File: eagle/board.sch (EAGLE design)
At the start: 11 parts, among them J1 M20X2SHROUDED

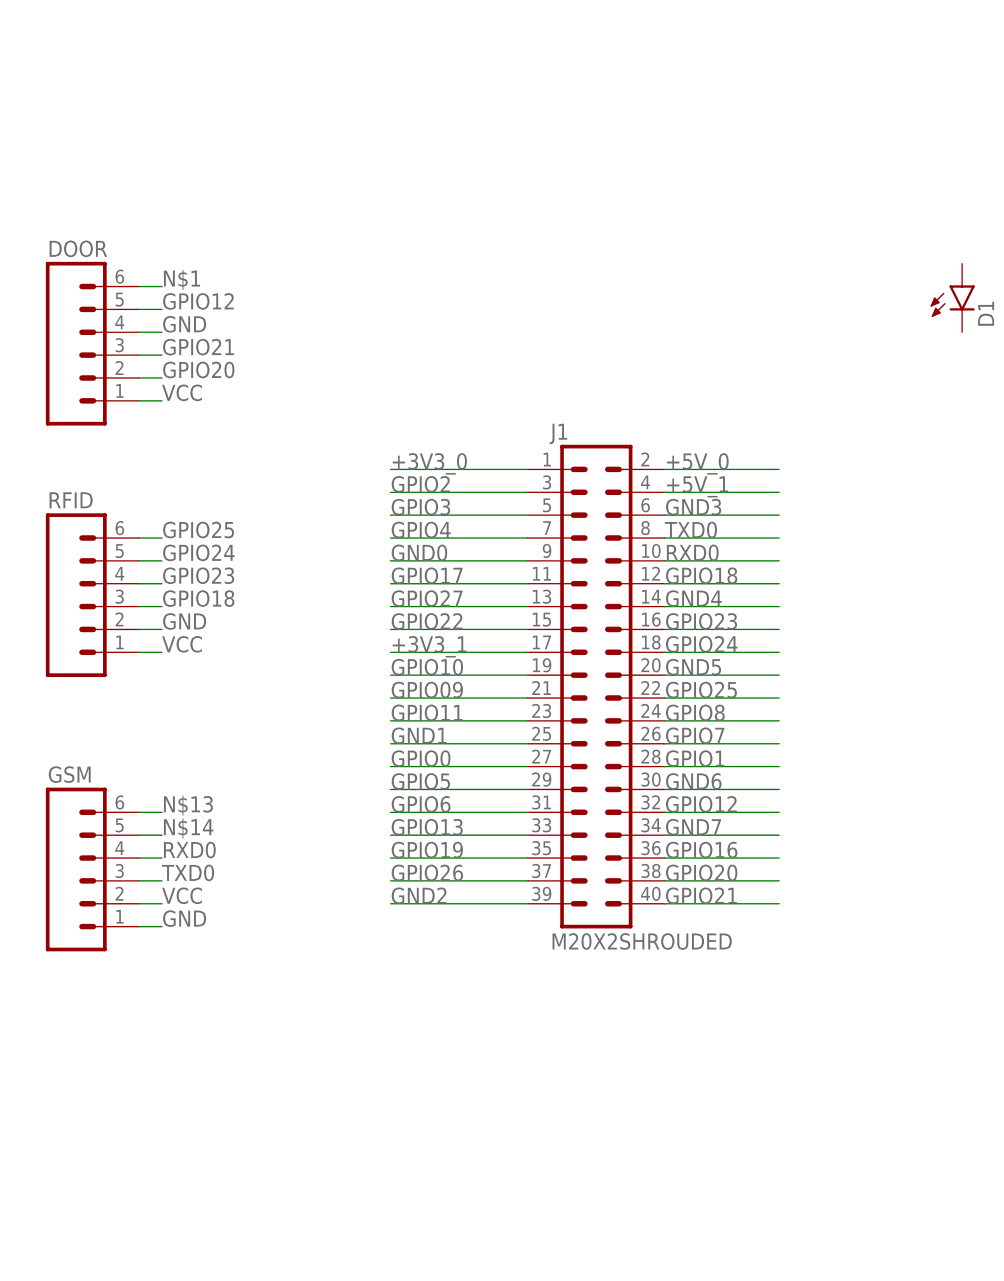
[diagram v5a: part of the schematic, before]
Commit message: Rename nets to match signal
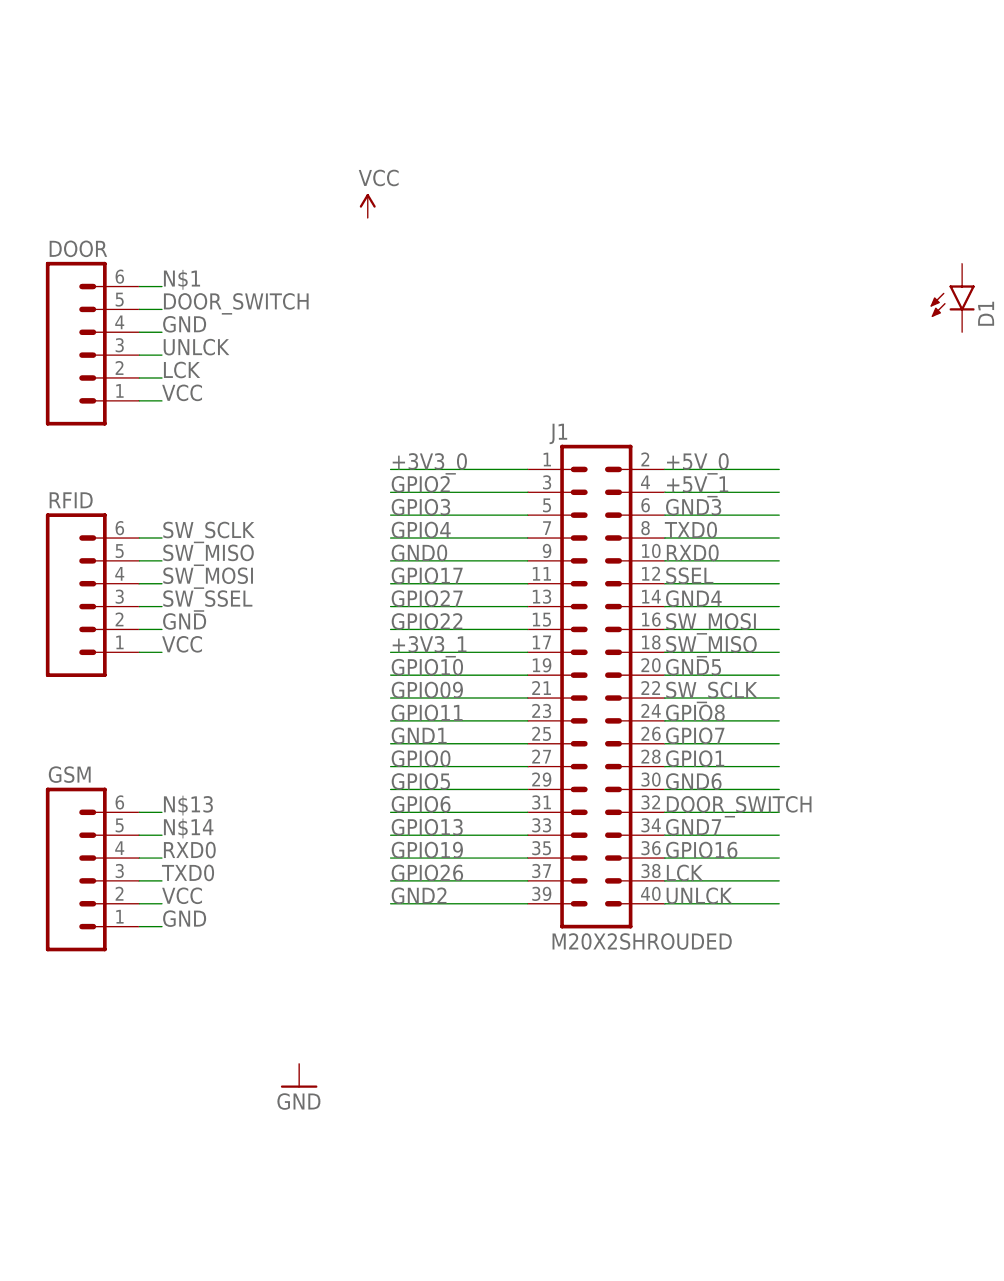
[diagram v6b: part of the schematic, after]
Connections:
- net GPIO12 renamed DOOR_SWITCH
- net GPIO20 renamed LCK
- net GPIO21 renamed UNLCK
- net GPIO23 renamed SW_MOSI
- net GPIO24 renamed SW_MISO
- net GPIO25 renamed SW_SCLK
- removed net GPIO18: J1.12, RFID.3
- new net SSEL: J1.12
- new net SW_SSEL: RFID.3
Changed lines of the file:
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@@
 <part name="C1" library="SparkFun-Passives" deviceset="CAP" device="PTH" value="10nF"/>
 <part name="C2" library="SparkFun-Passives" deviceset="CAP" device="PTH" value="10nF"/>
+<part name="SUPPLY1" library="SparkFun-Aesthetics" deviceset="VCC" device=""/>
+<part name="GND1" library="SparkFun-Aesthetics" deviceset="GND" device=""/>
 </parts>
 <sheets>
@@
 <instance part="C1" gate="G$1" x="119.38" y="55.88" rot="R270"/>
 <instance part="C2" gate="G$1" x="187.96" y="53.34" rot="R90"/>
+<instance part="SUPPLY1" gate="G$1" x="43.18" y="142.24"/>
+<instance part="GND1" gate="1" x="35.56" y="45.72"/>
 </instances>
 <busses>
@@
 </segment>
 </net>
-<net name="GPIO18" class="0">
+<net name="SSEL" class="0">
 <segment>
 <pinref part="J1" gate="G$1" pin="12"/>
@@
 <label x="76.2" y="101.6" size="1.778" layer="95"/>
 </segment>
-<segment>
-<pinref part="RFID" gate="G$1" pin="3"/>
-<wire x1="17.78" y1="99.06" x2="20.32" y2="99.06" width="0.1524" layer="91"/>
-<label x="20.32" y="99.06" size="1.778" layer="95"/>
-</segment>
-</net>
-<net name="GPIO23" class="0">
+</net>
+<net name="SW_MOSI" class="0">
 <segment>
 <pinref part="J1" gate="G$1" pin="16"/>
@@
 </segment>
 </net>
-<net name="GPIO24" class="0">
+<net name="SW_MISO" class="0">
 <segment>
 <pinref part="J1" gate="G$1" pin="18"/>
@@
 </segment>
 </net>
-<net name="GPIO25" class="0">
+<net name="SW_SCLK" class="0">
 <segment>
 <pinref part="J1" gate="G$1" pin="22"/>
@@
 </segment>
 </net>
-<net name="GPIO12" class="0">
+<net name="DOOR_SWITCH" class="0">
 <segment>
 <pinref part="J1" gate="G$1" pin="32"/>
@@
 </segment>
 </net>
-<net name="GPIO20" class="0">
+<net name="LCK" class="0">
 <segment>
 <pinref part="J1" gate="G$1" pin="38"/>
@@
 </segment>
 </net>
-<net name="GPIO21" class="0">
+<net name="UNLCK" class="0">
 <segment>
 <pinref part="J1" gate="G$1" pin="40"/>
@@
 </segment>
 </net>
+<net name="SW_SSEL" class="0">
+<segment>
+<pinref part="RFID" gate="G$1" pin="3"/>
+<wire x1="17.78" y1="99.06" x2="20.32" y2="99.06" width="0.1524" layer="91"/>
+<label x="20.32" y="99.06" size="1.778" layer="95"/>
+</segment>
+</net>

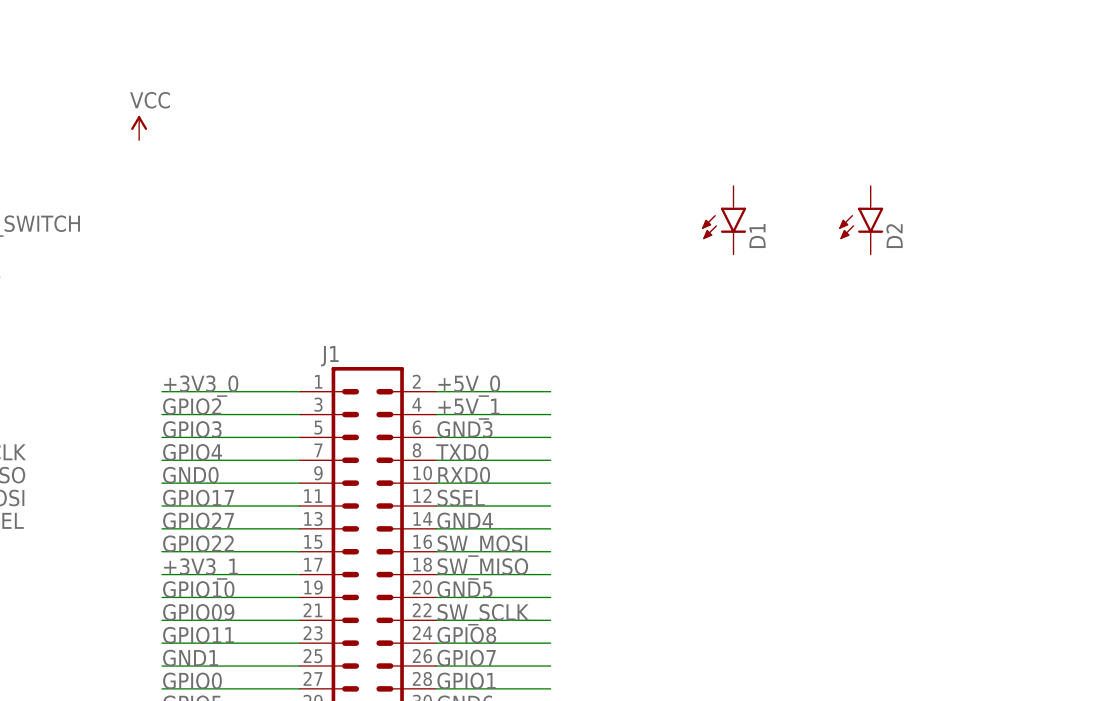
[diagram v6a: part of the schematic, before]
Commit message: Connect LEDs
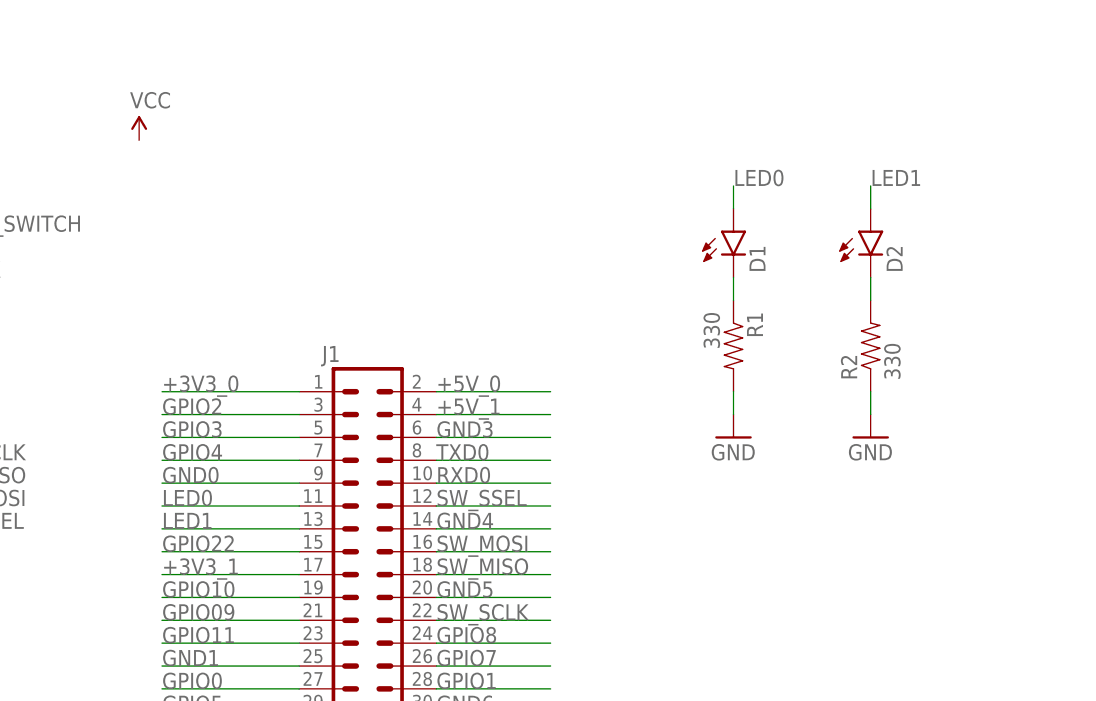
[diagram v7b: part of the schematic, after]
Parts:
- added R1, R2: 330, SparkFun-Passives:RESISTORPTH-1/4W
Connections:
- removed net GPIO17: J1.11
- removed net GPIO27: J1.13
- removed net SSEL: J1.12
- new net LED0: D1.A, J1.11
- new net LED1: D2.A, J1.13
- new net N$2: D1.C, R1.1
- new net N$3: D2.C, R2.2
- net GND: now also R1.2, R2.1
- net SW_SSEL: now also J1.12
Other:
- moved on the sheet: D1, D2
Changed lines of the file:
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@@
 <part name="SUPPLY1" library="SparkFun-Aesthetics" deviceset="VCC" device=""/>
 <part name="GND1" library="SparkFun-Aesthetics" deviceset="GND" device=""/>
+<part name="R1" library="SparkFun-Passives" deviceset="RESISTOR" device="PTH-1/4W" value="330"/>
+<part name="R2" library="SparkFun-Passives" deviceset="RESISTOR" device="PTH-1/4W" value="330"/>
+<part name="GND2" library="SparkFun-Aesthetics" deviceset="GND" device=""/>
+<part name="GND3" library="SparkFun-Aesthetics" deviceset="GND" device=""/>
 </parts>
 <sheets>
@@
 <instance part="FRAME1" gate="G$1" x="0" y="0"/>
 <instance part="FRAME1" gate="V" x="147.32" y="0"/>
-<instance part="D1" gate="G$1" x="109.22" y="134.62"/>
-<instance part="D2" gate="G$1" x="124.46" y="134.62"/>
+<instance part="D1" gate="G$1" x="109.22" y="132.08"/>
+<instance part="D2" gate="G$1" x="124.46" y="132.08"/>
 <instance part="DOOR" gate="G$1" x="12.7" y="127"/>
 <instance part="RFID" gate="G$1" x="12.7" y="99.06"/>
@@
 <instance part="SUPPLY1" gate="G$1" x="43.18" y="142.24"/>
 <instance part="GND1" gate="1" x="35.56" y="45.72"/>
+<instance part="R1" gate="G$1" x="109.22" y="119.38" rot="R270"/>
+<instance part="R2" gate="G$1" x="124.46" y="119.38" rot="R90"/>
+<instance part="GND2" gate="1" x="109.22" y="109.22"/>
+<instance part="GND3" gate="1" x="124.46" y="109.22"/>
 </instances>
 <busses>
@@
 </segment>
 </net>
-<net name="SSEL" class="0">
-<segment>
-<pinref part="J1" gate="G$1" pin="12"/>
-<wire x1="76.2" y1="101.6" x2="88.9" y2="101.6" width="0.1524" layer="91"/>
-<label x="76.2" y="101.6" size="1.778" layer="95"/>
-</segment>
-</net>
 <net name="SW_MOSI" class="0">
 <segment>
@@
 </segment>
 </net>
-<net name="GPIO17" class="0">
-<segment>
-<pinref part="J1" gate="G$1" pin="11"/>
-<wire x1="60.96" y1="101.6" x2="45.72" y2="101.6" width="0.1524" layer="91"/>
-<label x="45.72" y="101.6" size="1.778" layer="95"/>
-</segment>
-</net>
-<net name="GPIO27" class="0">
-<segment>
-<pinref part="J1" gate="G$1" pin="13"/>
-<wire x1="60.96" y1="99.06" x2="45.72" y2="99.06" width="0.1524" layer="91"/>
-<label x="45.72" y="99.06" size="1.778" layer="95"/>
-</segment>
-</net>
 <net name="GPIO22" class="0">
 <segment>
@@
 <wire x1="17.78" y1="63.5" x2="20.32" y2="63.5" width="0.1524" layer="91"/>
 <label x="20.32" y="63.5" size="1.778" layer="95"/>
+</segment>
+<segment>
+<pinref part="R1" gate="G$1" pin="2"/>
+<pinref part="GND2" gate="1" pin="GND"/>
+<wire x1="109.22" y1="114.3" x2="109.22" y2="111.76" width="0.1524" layer="91"/>
+</segment>
+<segment>
+<pinref part="R2" gate="G$1" pin="1"/>
+<pinref part="GND3" gate="1" pin="GND"/>
+<wire x1="124.46" y1="114.3" x2="124.46" y2="111.76" width="0.1524" layer="91"/>
 </segment>
 </net>
@@
 <label x="20.32" y="99.06" size="1.778" layer="95"/>
 </segment>
-</net>
+<segment>
+<pinref part="J1" gate="G$1" pin="12"/>
+<wire x1="76.2" y1="101.6" x2="88.9" y2="101.6" width="0.1524" layer="91"/>
+<label x="76.2" y="101.6" size="1.778" layer="95"/>
+</segment>
+</net>
+<net name="LED0" class="0">
+<segment>
+<pinref part="D1" gate="G$1" pin="A"/>
+<wire x1="109.22" y1="134.62" x2="109.22" y2="137.16" width="0.1524" layer="91"/>
+<label x="109.22" y="137.16" size="1.778" layer="95"/>
+</segment>
+<segment>
+<pinref part="J1" gate="G$1" pin="11"/>
+<wire x1="60.96" y1="101.6" x2="45.72" y2="101.6" width="0.1524" layer="91"/>
+<label x="45.72" y="101.6" size="1.778" layer="95"/>
+</segment>
+</net>
+<net name="LED1" class="0">
+<segment>
+<pinref part="D2" gate="G$1" pin="A"/>
+<wire x1="124.46" y1="134.62" x2="124.46" y2="137.16" width="0.1524" layer="91"/>
+<label x="124.46" y="137.16" size="1.778" layer="95"/>
+</segment>
+<segment>
+<pinref part="J1" gate="G$1" pin="13"/>
+<wire x1="60.96" y1="99.06" x2="45.72" y2="99.06" width="0.1524" layer="91"/>
+<label x="45.72" y="99.06" size="1.778" layer="95"/>
+</segment>
+</net>
+<net name="N$2" class="0">
+<segment>
+<pinref part="D1" gate="G$1" pin="C"/>
+<pinref part="R1" gate="G$1" pin="1"/>
+<wire x1="109.22" y1="127" x2="109.22" y2="124.46" width="0.1524" layer="91"/>
+</segment>
+</net>
+<net name="N$3" class="0">
+<segment>
+<pinref part="D2" gate="G$1" pin="C"/>
+<pinref part="R2" gate="G$1" pin="2"/>
+<wire x1="124.46" y1="127" x2="124.46" y2="124.46" width="0.1524" layer="91"/>
+</segment>
+</net>
